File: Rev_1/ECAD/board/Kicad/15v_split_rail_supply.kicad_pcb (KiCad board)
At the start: 2 copper layers, 18 parts, among them Q1 IPP029N15NM6, U1 LM3478MA

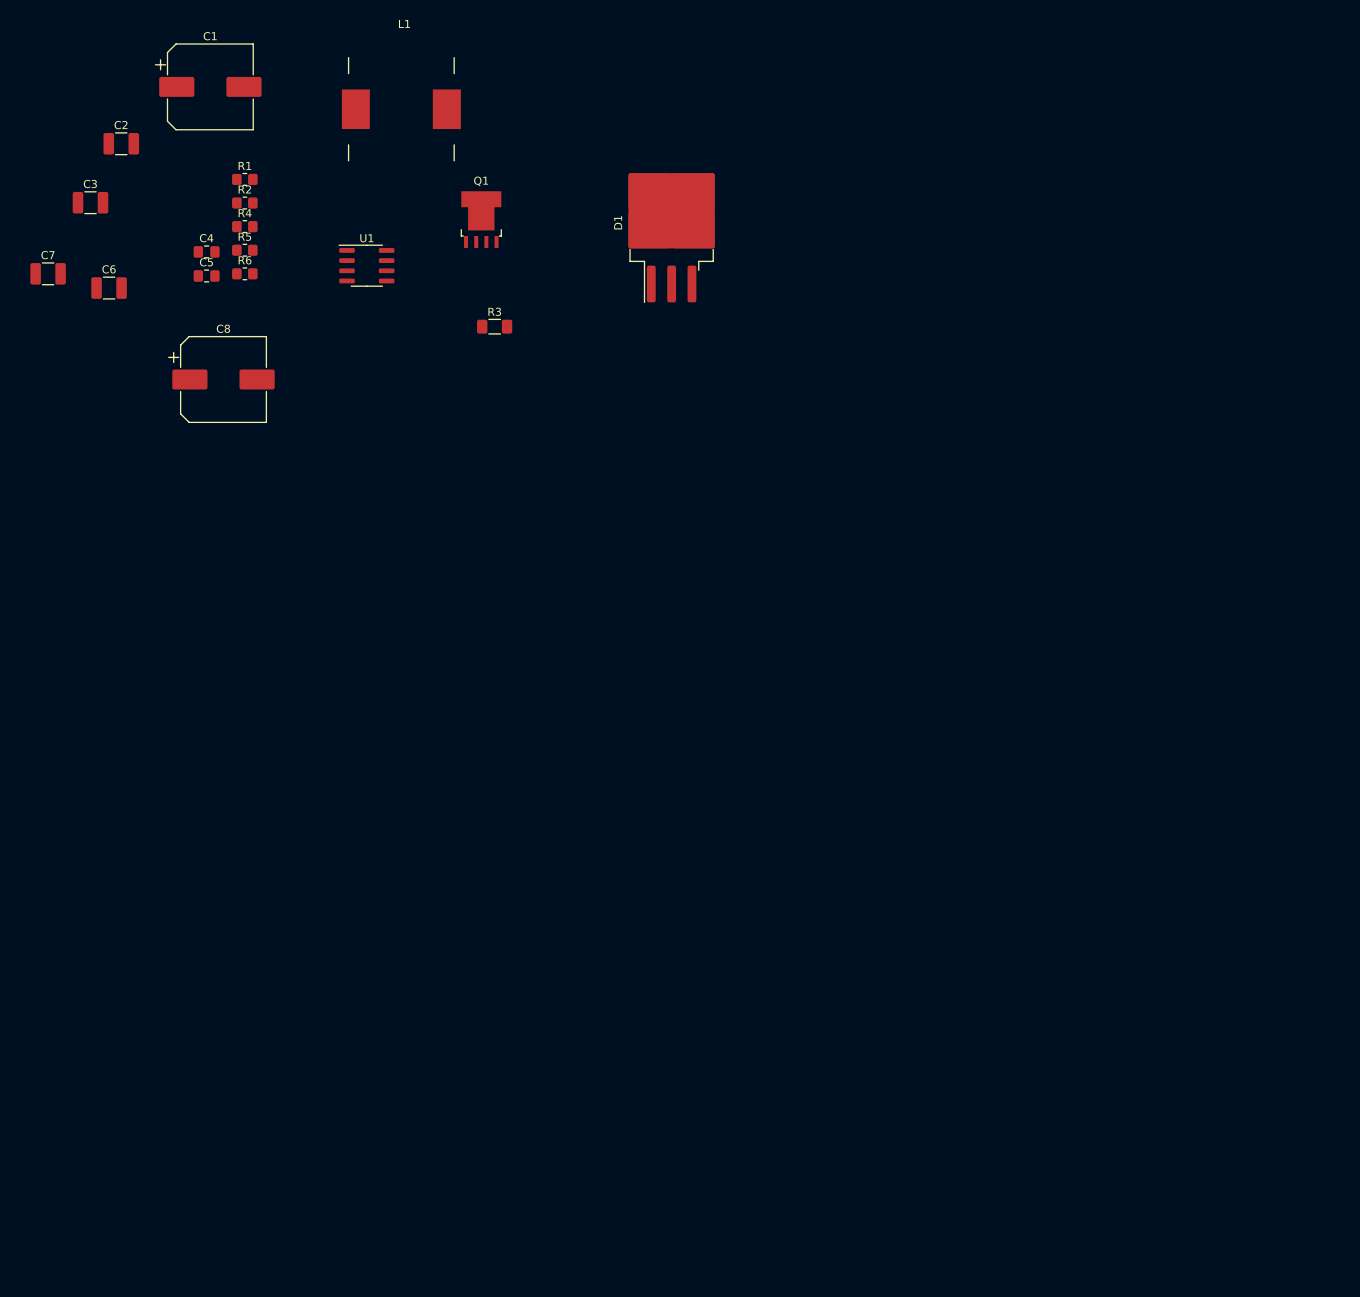
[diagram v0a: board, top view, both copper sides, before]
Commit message: Made the logic for Overcurrent
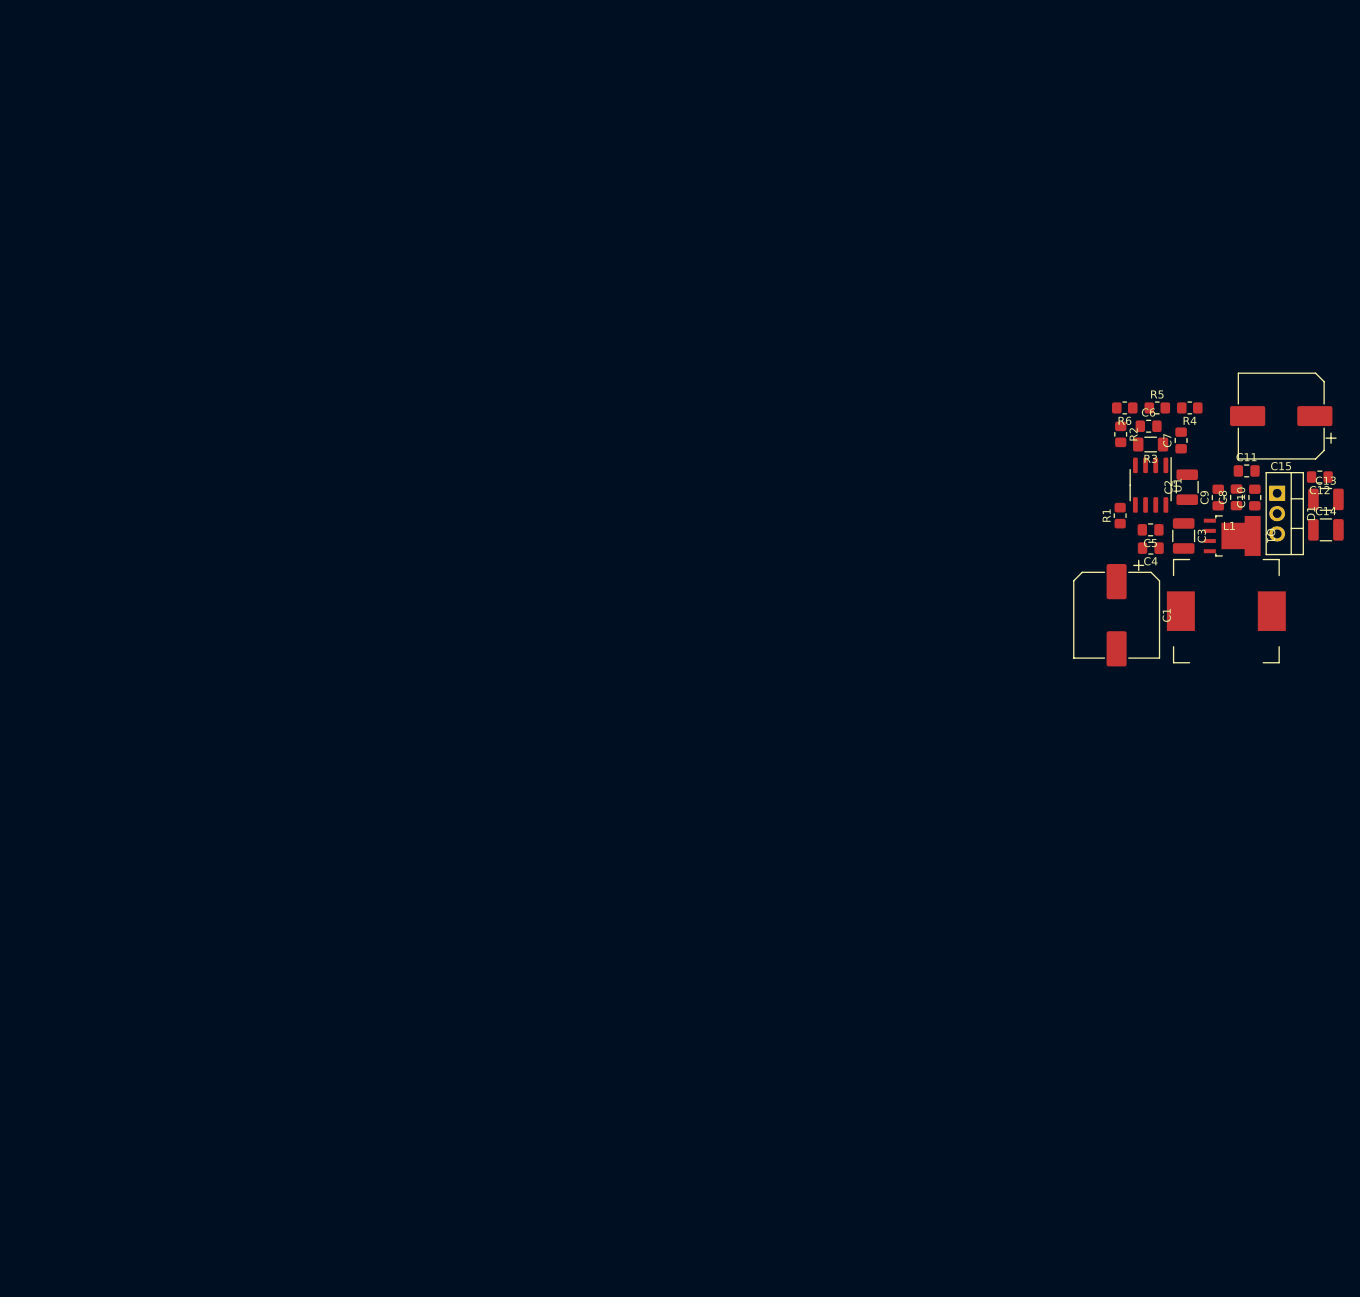
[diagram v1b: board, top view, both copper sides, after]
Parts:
- added C10: 1u, Capacitor_SMD:C_0805_2012Metric_Pad1.18x1.45mm_HandSolder, F.Cu at (189.0, 78.0)
- added C11: 100n, Capacitor_SMD:C_0805_2012Metric_Pad1.18x1.45mm_HandSolder, F.Cu at (188.0, 74.7)
- added C12: 1u, Capacitor_SMD:C_0805_2012Metric_Pad1.18x1.45mm_HandSolder, F.Cu at (197.1, 75.4)
- added C4: 1u, Capacitor_SMD:C_0805_2012Metric_Pad1.18x1.45mm_HandSolder, F.Cu at (176.0, 84.3)
- added C5: 100n, Capacitor_SMD:C_0805_2012Metric_Pad1.18x1.45mm_HandSolder, F.Cu at (176.0, 82.0)
- added C8: 100n, Capacitor_SMD:C_0805_2012Metric_Pad1.18x1.45mm_HandSolder, F.Cu at (186.7, 78.0)
- added C9: 100n, Capacitor_SMD:C_0805_2012Metric_Pad1.18x1.45mm_HandSolder, F.Cu at (184.4, 78.0)
- D1: footprint Package_TO_SOT_SMD:TO-263-3_TabPin2 -> Package_TO_SOT_THT:TO-220-3_Vertical
- moved C14 162.9 mm to (197.9, 82.0)
- moved C13 154.4 mm to (197.9, 78.2)
- moved C3 142.9 mm to (180.1, 82.8), turned to -90 degrees
- moved C2 140.0 mm to (180.5, 76.7), turned to 90 degrees
- moved C15 132.3 mm to (192.3, 67.8), turned to 180 degrees
- moved C1 131.1 mm to (171.7, 92.7), turned to -90 degrees
- moved C7 123.5 mm to (179.8, 70.9), turned to 90 degrees
- moved L1 120.7 mm to (185.4, 92.2)
- moved R4 120.3 mm to (180.8, 66.8), turned to 180 degrees
- moved C6 119.7 mm to (175.7, 69.1)
- moved R1 117.2 mm to (172.1, 80.3), turned to 90 degrees
- moved R5 115.7 mm to (176.8, 66.8)
- moved R2 113.2 mm to (172.2, 70.1), turned to -90 degrees
- moved R6 111.3 mm to (172.7, 66.8), turned to 180 degrees
- moved U1 101.7 mm to (176.0, 76.5), turned to -90 degrees
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- renumbered C6 to C13, C7 to C14, C8 to C15, C4 to C6, C5 to C7
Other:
- copper layers 2 -> 4

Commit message: Components for 15V regulator are placed
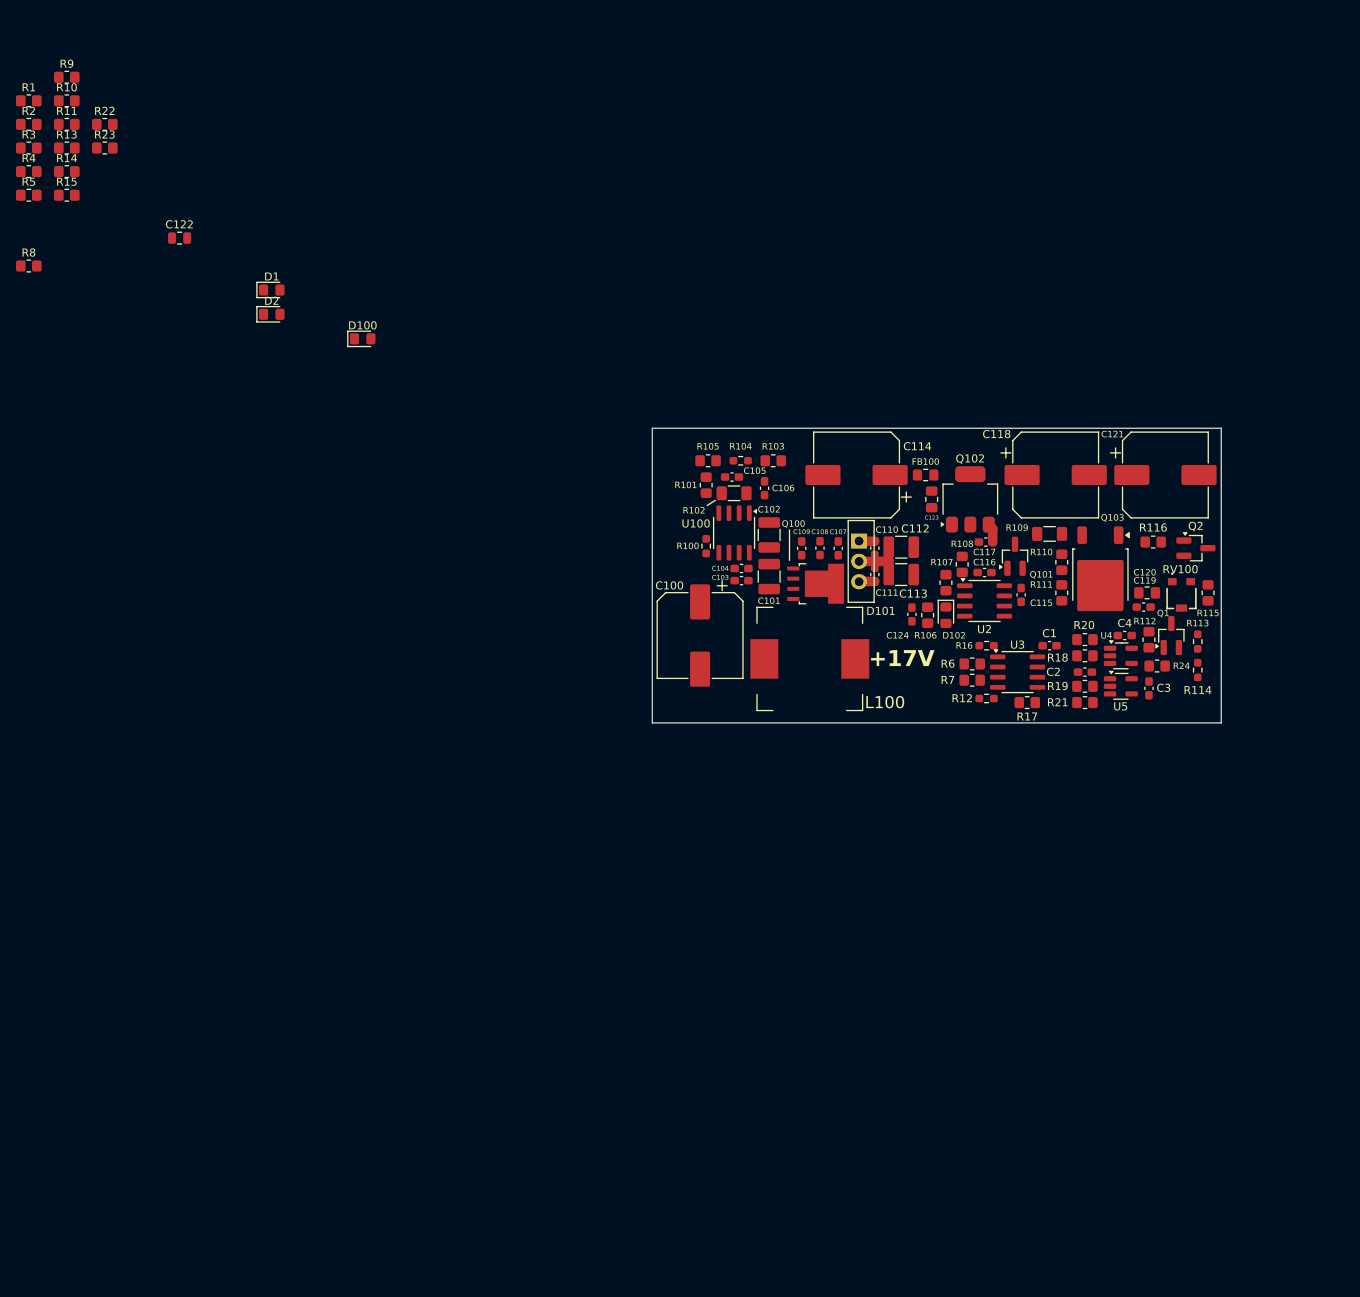
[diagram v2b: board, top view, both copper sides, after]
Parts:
- removed C10, C12: 1u, Capacitor_SMD:C_0805_2012Metric_Pad1.18x1.45mm_HandSolder
- removed C11, C5, C8, C9: 100n, Capacitor_SMD:C_0805_2012Metric_Pad1.18x1.45mm_HandSolder
- removed C13, C14: 47u, Capacitor_SMD:C_1210_3225Metric_Pad1.33x2.70mm_HandSolder
- removed C15: 220u, Capacitor_SMD:CP_Elec_10x10.5
- removed C6: 2.2n, Capacitor_SMD:C_0805_2012Metric_Pad1.18x1.45mm_HandSolder
- removed C7: 220n, Capacitor_SMD:C_0805_2012Metric_Pad1.18x1.45mm_HandSolder
- removed L1: 5.6u, filip:IHLP5050FD
- removed U1: LM3478MA, Package_SO:SOIC-8_3.9x4.9mm_P1.27mm
- added C100: 220u, Capacitor_SMD:CP_Elec_10x10.5, F.Cu at (119.6, 95.2)
- added C101: 47u, Capacitor_SMD:C_1210_3225Metric_Pad1.33x2.70mm_HandSolder, F.Cu at (128.3, 87.9)
- added C102: 47u, Capacitor_SMD:C_1210_3225Metric_Pad1.33x2.70mm_HandSolder, F.Cu at (128.3, 82.7)
- added C103: 1u, Capacitor_SMD:C_0603_1608Metric_Pad1.08x0.95mm_HandSolder, F.Cu at (124.8, 88.4)
- added C104: 100n, Capacitor_SMD:C_0603_1608Metric_Pad1.08x0.95mm_HandSolder, F.Cu at (124.8, 86.9)
- added C105: 2.2n, Capacitor_SMD:C_0603_1608Metric_Pad1.08x0.95mm_HandSolder, F.Cu at (123.6, 75.4)
- added C106: 220n, Capacitor_SMD:C_0603_1608Metric_Pad1.08x0.95mm_HandSolder, F.Cu at (127.7, 76.8)
- added C107: 100n, Capacitor_SMD:C_0603_1608Metric_Pad1.08x0.95mm_HandSolder, F.Cu at (136.9, 84.3)
- added C108: 100n, Capacitor_SMD:C_0603_1608Metric_Pad1.08x0.95mm_HandSolder, F.Cu at (134.6, 84.3)
- added C109: 1u, Capacitor_SMD:C_0603_1608Metric_Pad1.08x0.95mm_HandSolder, F.Cu at (132.3, 84.3)
- added C110: 1u, Capacitor_SMD:C_0603_1608Metric_Pad1.08x0.95mm_HandSolder, F.Cu at (141.5, 84.3)
- added C111: 100n, Capacitor_SMD:C_0603_1608Metric_Pad1.08x0.95mm_HandSolder, F.Cu at (141.5, 87.6)
- added C112: 47u, Capacitor_SMD:C_1210_3225Metric_Pad1.33x2.70mm_HandSolder, F.Cu at (144.8, 84.2)
- added C113: 47u, Capacitor_SMD:C_1210_3225Metric_Pad1.33x2.70mm_HandSolder, F.Cu at (144.8, 87.6)
- added C114: 220u, Capacitor_SMD:CP_Elec_10x10.5, F.Cu at (139.2, 75.2)
- added C115: 100n, Capacitor_SMD:C_0603_1608Metric_Pad1.08x0.95mm_HandSolder, F.Cu at (159.8, 90.2)
- added C116: 10p, Capacitor_SMD:C_0603_1608Metric_Pad1.08x0.95mm_HandSolder, F.Cu at (155.2, 87.4)
- added C117: 100n, Capacitor_SMD:C_0603_1608Metric_Pad1.08x0.95mm_HandSolder, F.Cu at (155.3, 83.6)
- added C118: 100u, Capacitor_SMD:CP_Elec_10x10.5, F.Cu at (164.1, 75.2)
- added C119: 1u, Capacitor_SMD:C_0603_1608Metric_Pad1.08x0.95mm_HandSolder, F.Cu at (175.1, 91.7)
- added C120: 10u, Capacitor_SMD:C_0805_2012Metric_Pad1.18x1.45mm_HandSolder, F.Cu at (175.5, 89.9)
- added C121: 220u, Capacitor_SMD:CP_Elec_10x10.5, F.Cu at (177.8, 75.2)
- added C122: 100n, Capacitor_SMD:C_0805_2012Metric, F.Cu at (54.6, 45.6)
- added C123: 1u, Capacitor_SMD:C_0805_2012Metric_Pad1.18x1.45mm_HandSolder, F.Cu at (148.6, 78.2)
- added C124: 100n, Capacitor_SMD:C_0603_1608Metric_Pad1.08x0.95mm_HandSolder, F.Cu at (146.1, 92.6)
- added D100: D_TVS, Diode_SMD:D_0805_2012Metric_Pad1.15x1.40mm_HandSolder, F.Cu at (77.5, 58.2)
- added D101: WNS40H100CB, Package_TO_SOT_THT:TO-220-3_Vertical, F.Cu at (139.5, 83.4)
- added D102: 5V6, Diode_SMD:D_0805_2012Metric_Pad1.15x1.40mm_HandSolder, F.Cu at (150.4, 92.7)
- added D2: RED, LED_SMD:LED_0805_2012Metric_Pad1.15x1.40mm_HandSolder, F.Cu at (66.1, 55.1)
- added FB100: 100, Inductor_SMD:L_0805_2012Metric_Pad1.15x1.40mm_HandSolder, F.Cu at (147.8, 75.2)
- added L100: 5.6u, filip:L_IHLP5050FD_5.0x5.0mm_Shielded, F.Cu at (133.3, 98.2)
- added Q100: IPP029N15NM6, filip:TO-263-5_TabPin1-HandSoldered, F.Cu at (133.8, 88.8)
- added Q101: NPN, Package_TO_SOT_SMD:SOT-23_Handsoldering, F.Cu at (159.0, 85.3)
- added Q102: NPN, Package_TO_SOT_SMD:SOT-223-3_TabPin2, F.Cu at (153.4, 78.2)
- added Q103: PMOS, Package_TO_SOT_SMD:TO-252-2, F.Cu at (169.7, 87.7)
- added Q2: NPN, Package_TO_SOT_SMD:SOT-23_Handsoldering, F.Cu at (181.6, 84.3)
- added R10: 1k, Resistor_SMD:R_0805_2012Metric_Pad1.20x1.40mm_HandSolder, F.Cu at (40.5, 28.4)
- added R100: 13k, Resistor_SMD:R_0603_1608Metric_Pad0.98x0.95mm_HandSolder, F.Cu at (120.4, 84.1)
- added R101: 10k, Resistor_SMD:R_0805_2012Metric_Pad1.20x1.40mm_HandSolder, F.Cu at (120.4, 76.5)
- added R102: 20m, Resistor_SMD:R_1206_3216Metric_Pad1.30x1.75mm_HandSolder, F.Cu at (123.9, 77.5)
- added R103: 100k, Resistor_SMD:R_0805_2012Metric_Pad1.20x1.40mm_HandSolder, F.Cu at (128.8, 73.4)
- added R104: 27k, Resistor_SMD:R_0603_1608Metric_Pad0.98x0.95mm_HandSolder, F.Cu at (124.7, 73.4)
- added R105: 10k, Resistor_SMD:R_0805_2012Metric_Pad1.20x1.40mm_HandSolder, F.Cu at (120.6, 73.4)
- added R106: 100k, Resistor_SMD:R_0805_2012Metric_Pad1.20x1.40mm_HandSolder, F.Cu at (148.1, 92.7)
- added R107: 10k, Resistor_SMD:R_0805_2012Metric_Pad1.20x1.40mm_HandSolder, F.Cu at (150.4, 88.6)
- added R108: 10, Resistor_SMD:R_0805_2012Metric_Pad1.20x1.40mm_HandSolder, F.Cu at (152.4, 86.4)
- added R109: 20m, Resistor_SMD:R_1206_3216Metric_Pad1.30x1.75mm_HandSolder, F.Cu at (163.3, 82.5)
- added R11: 1k, Resistor_SMD:R_0805_2012Metric_Pad1.20x1.40mm_HandSolder, F.Cu at (40.5, 31.4)
- added R110: 10k, Resistor_SMD:R_0805_2012Metric_Pad1.20x1.40mm_HandSolder, F.Cu at (164.8, 86.1)
- added R111: 100k, Resistor_SMD:R_0805_2012Metric_Pad1.20x1.40mm_HandSolder, F.Cu at (164.8, 89.9)
- added R112: 100, Resistor_SMD:R_0805_2012Metric_Pad1.20x1.40mm_HandSolder, F.Cu at (175.7, 95.8)
- added R113: ?, Resistor_SMD:R_0603_1608Metric_Pad0.98x0.95mm_HandSolder, F.Cu at (181.8, 96.0)
- added R114: ?, Resistor_SMD:R_0603_1608Metric_Pad0.98x0.95mm_HandSolder, F.Cu at (181.8, 99.6)
- added R115: 100, Resistor_SMD:R_0805_2012Metric_Pad1.20x1.40mm_HandSolder, F.Cu at (183.1, 89.9)
- added R116: 100, Resistor_SMD:R_0805_2012Metric_Pad1.20x1.40mm_HandSolder, F.Cu at (176.3, 83.6)
- added R12: 50k, Resistor_SMD:R_0603_1608Metric_Pad0.98x0.95mm_HandSolder, F.Cu at (155.4, 103.1)
- added R13: 1k, Resistor_SMD:R_0805_2012Metric_Pad1.20x1.40mm_HandSolder, F.Cu at (40.5, 34.3)
- added R14: 10k, Resistor_SMD:R_0805_2012Metric_Pad1.20x1.40mm_HandSolder, F.Cu at (40.5, 37.3)
- added R15: 10k, Resistor_SMD:R_0805_2012Metric_Pad1.20x1.40mm_HandSolder, F.Cu at (40.5, 40.2)
- added R16: 50k, Resistor_SMD:R_0603_1608Metric_Pad0.98x0.95mm_HandSolder, F.Cu at (155.4, 96.5)
- added R17: 1k, Resistor_SMD:R_0805_2012Metric_Pad1.20x1.40mm_HandSolder, F.Cu at (160.5, 103.6)
- added R18: 1k, Resistor_SMD:R_0805_2012Metric_Pad1.20x1.40mm_HandSolder, F.Cu at (167.7, 97.8)
- added R19: 1k, Resistor_SMD:R_0805_2012Metric_Pad1.20x1.40mm_HandSolder, F.Cu at (167.7, 101.6)
- added R20: 10k, Resistor_SMD:R_0805_2012Metric_Pad1.20x1.40mm_HandSolder, F.Cu at (167.7, 95.8)
- added R21: 10k, Resistor_SMD:R_0805_2012Metric_Pad1.20x1.40mm_HandSolder, F.Cu at (167.7, 103.6)
- added R22: 4k7, Resistor_SMD:R_0805_2012Metric_Pad1.20x1.40mm_HandSolder, F.Cu at (45.2, 31.4)
- added R23: 4k7, Resistor_SMD:R_0805_2012Metric_Pad1.20x1.40mm_HandSolder, F.Cu at (45.2, 34.3)
- added R24: 1K, Resistor_SMD:R_0805_2012Metric_Pad1.20x1.40mm_HandSolder, F.Cu at (176.8, 99.1)
- added R7: 1k, Resistor_SMD:R_0805_2012Metric_Pad1.20x1.40mm_HandSolder, F.Cu at (153.7, 100.8)
- added R8: 1k, Resistor_SMD:R_0805_2012Metric_Pad1.20x1.40mm_HandSolder, F.Cu at (35.7, 49.1)
- added R9: 10k, Resistor_SMD:R_0805_2012Metric_Pad1.20x1.40mm_HandSolder, F.Cu at (40.5, 25.5)
- added RV100: 10k, filip:Potentiometer_SMD_Trimmer_PVG3_3.6x3, F.Cu at (179.8, 90.2)
- added U100: LM3478MA, Package_SO:SOIC-8_3.9x4.9mm_P1.27mm, F.Cu at (123.9, 82.4)
- added U2: LM358, Package_SO:SOIC-8_3.9x4.9mm_P1.27mm, F.Cu at (155.2, 90.9)
- added U3: LM358, Package_SO:SOIC-8_3.9x4.9mm_P1.27mm, F.Cu at (159.3, 99.8)
- added U4: SN74AHC1G02DBVR, Package_TO_SOT_SMD:SOT-23-5_HandSoldering, F.Cu at (172.2, 97.8)
- added U5: SN74AHC1G02DBVR, Package_TO_SOT_SMD:SOT-23-5_HandSoldering, F.Cu at (172.2, 101.6)
- C1: value 220u -> 100n; footprint Capacitor_SMD:CP_Elec_10x10.5 -> Capacitor_SMD:C_0603_1608Metric_Pad1.08x0.95mm_HandSolder
- C2, C3: value 47u -> 100n; footprint Capacitor_SMD:C_1210_3225Metric_Pad1.33x2.70mm_HandSolder -> Capacitor_SMD:C_0603_1608Metric_Pad1.08x0.95mm_HandSolder
- C4: value 1u -> 100n; footprint Capacitor_SMD:C_0805_2012Metric_Pad1.18x1.45mm_HandSolder -> Capacitor_SMD:C_0603_1608Metric_Pad1.08x0.95mm_HandSolder
- D1: value WNS40H100CB -> Green; footprint Package_TO_SOT_THT:TO-220-3_Vertical -> LED_SMD:LED_0805_2012Metric_Pad1.15x1.40mm_HandSolder
- Q1: value IPP029N15NM6 -> NPN; footprint filip:PSMN4R0 -> Package_TO_SOT_SMD:SOT-23_Handsoldering
- R1: value 13k -> 10k
- R2: value 10k -> 4k7
- R3: value 15.5m -> 10k; footprint Resistor_SMD:R_1206_3216Metric_Pad1.30x1.75mm_HandSolder -> Resistor_SMD:R_0805_2012Metric_Pad1.20x1.40mm_HandSolder
- R4: value 100k -> 1k
- R5: value 27k -> 1k
- R6: value 10k -> 1k
- moved R4 148.1 mm to (35.7, 37.3), turned to 0 degrees
- moved R1 145.9 mm to (35.7, 28.4), turned to 0 degrees
- moved R3 145.0 mm to (35.7, 34.3), turned to 0 degrees
- moved R5 143.5 mm to (35.7, 40.2)
- moved R2 141.9 mm to (35.7, 31.4), turned to 0 degrees
- moved D1 128.2 mm to (66.1, 52.1), turned to 0 degrees
- moved R6 37.3 mm to (153.7, 98.8), turned to 0 degrees
- moved C2 26.4 mm to (167.7, 99.8), turned to 0 degrees
- moved C3 19.5 mm to (175.7, 101.9), turned to 90 degrees
- moved Q1 14.5 mm to (178.5, 95.2), turned to 90 degrees
- moved C4 11.4 mm to (172.7, 95.2)
- moved C1 9.21 mm to (163.3, 96.5), turned to 180 degrees
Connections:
- C1 pad 1: /VIN -> GND
- C1 pad 2: GND -> +5V
- C2 pad 1: /VIN -> +5V
- C2 pad 2: GND -> /+15V DC-DC Converter/RESET
- C3 pad 1: /VIN -> +5V
- C4 pad 1: /VIN -> +5V
- D1 pad 1: /SW_POSB -> GND
- D1 pad 2: Net-(D1-K) -> Net-(D1-A)
- Q1 pad 1: /SW_POSB -> /+15V DC-DC Converter/SHUTDOWN
- Q1 pad 2: /DR_POSB -> /+15V DC-DC Converter/NPN_B
- Q1 pad 3: /S_ISEN_POSB -> GND
- R1 pad 1: /S_FA/SD_POSB -> +5V
- R1 pad 2: GND -> Net-(R1-Pad2)
- R2 pad 1: /S_COMP_POSB_R2 -> Net-(R2-Pad1)
- R2 pad 2: GND -> Net-(R2-Pad2)
- R3 pad 1: /S_ISEN_POSB -> Net-(R3-Pad1)
- R3 pad 2: GND -> Net-(R3-Pad2)
- R4 pad 1: Net-(D1-K) -> Net-(R4-Pad1)
- R4 pad 2: /S_DIV -> Net-(R10-Pad1)
- R5 pad 1: /S_DIV -> Net-(R5-Pad1)
- R5 pad 2: /S_FB_POSB -> /+15V DC-DC Converter/CURRENT_V_REF
- R6 pad 1: /S_FB_POSB -> /+15V DC-DC Converter/SHUNT_OUT
- R6 pad 2: GND -> /+15V DC-DC Converter/DIFF_NEG
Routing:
- net /+15V DC-DC Converter/LOOP_OUT: track 0.00 -> 5.78 mm
- net /+15V DC-DC Converter/SW: track 0.00 -> 3.95 mm
- net /+15V DC-DC Converter/SHUNT_IN: track 0.00 -> 2.39 mm
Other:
- board outline added: 71.1 x 36.8 mm
- board text added: "+17V"
